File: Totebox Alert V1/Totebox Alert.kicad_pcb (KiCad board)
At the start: 2 copper layers, 180 x 100 mm, 48 parts, among them J1 Conn_01x06, J10 Conn_01x02, J12 Conn_01x02, J3 Conn_01x06, J7 Conn_01x02, J8 Conn_01x02, J9 Conn_01x02, SW1 SW_SPST, U3 ESP32-DEVKITC-32UE

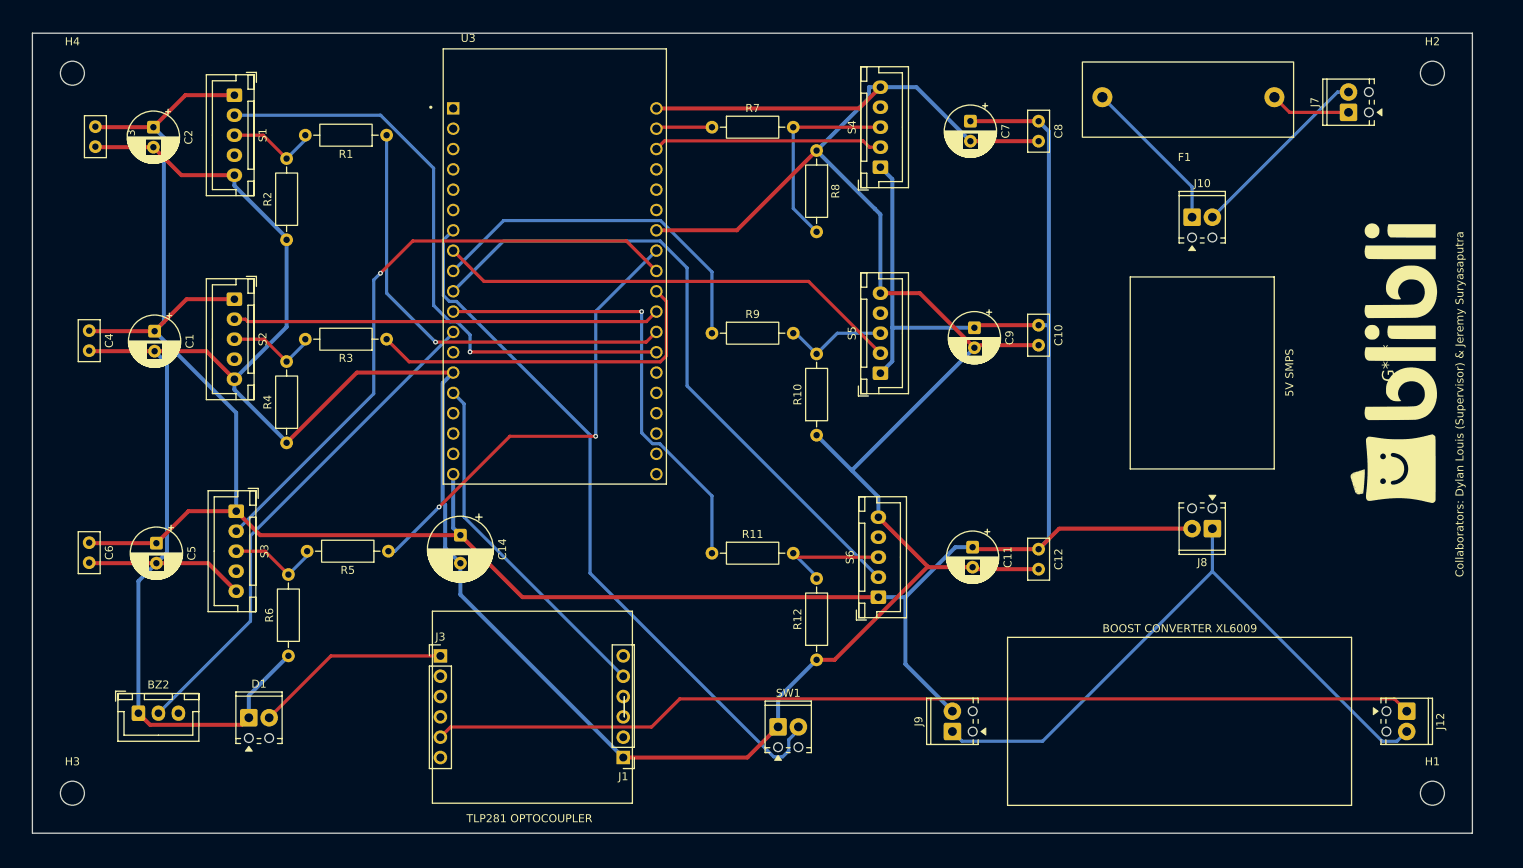
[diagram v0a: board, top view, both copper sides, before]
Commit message: move variables and constants to config.h files for easier configuration and maintenance add new alert tones for multitier floor units categorize mqtt topics to different floor and area units
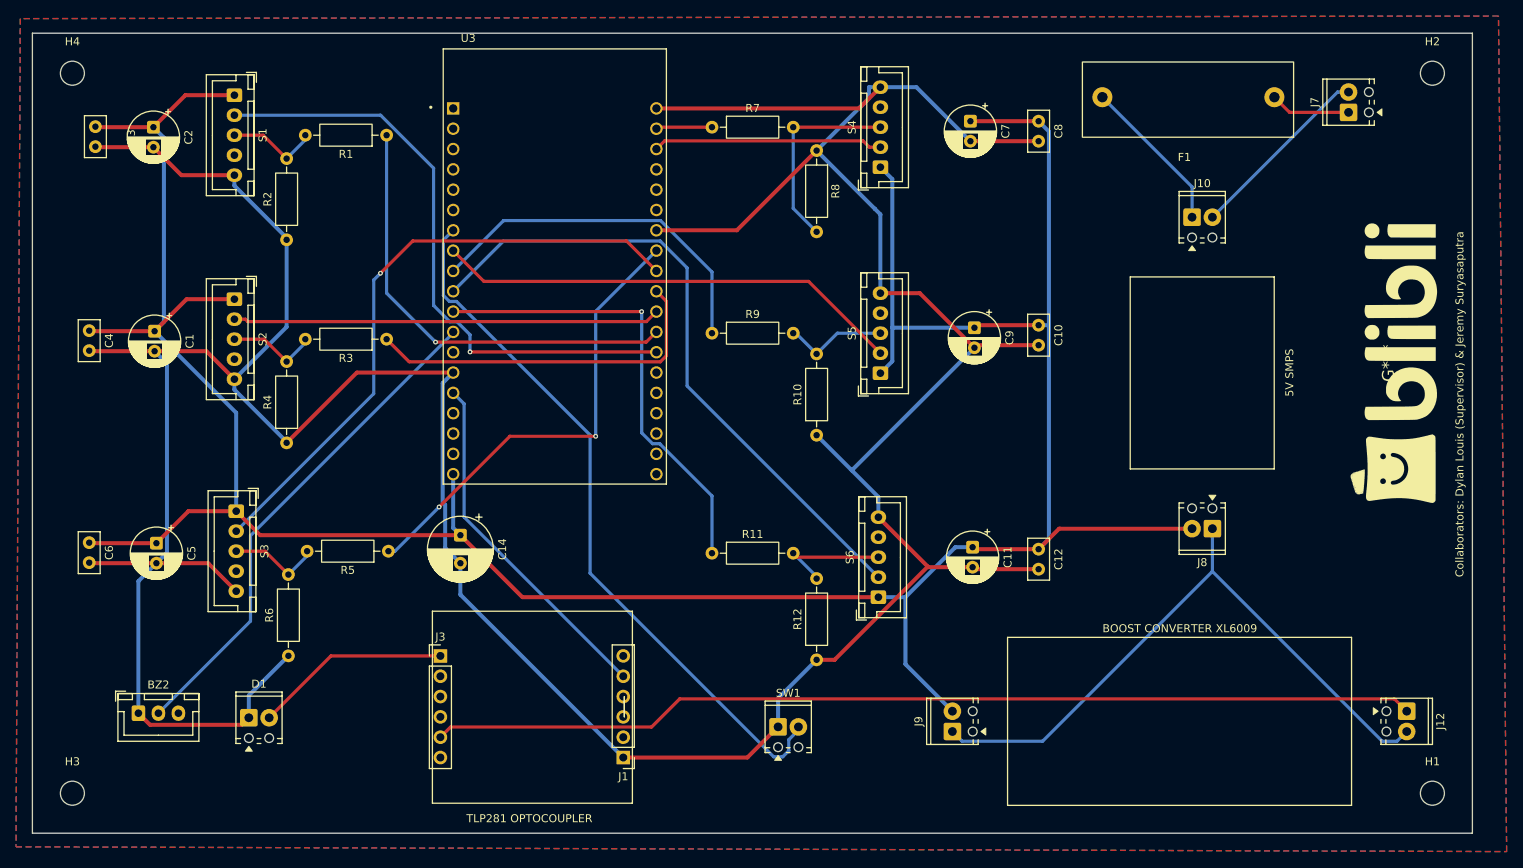
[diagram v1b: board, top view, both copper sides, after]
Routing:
- added copper zone on B.Cu, net (none)
- added copper zone on F.Cu, net (none)
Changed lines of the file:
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@@
+	)
+	(gr_rect
+		(start 86.5 98.5)
+		(end 111.5 122.5)
+		(stroke
+			(width 0.1)
+			(type default)
+		)
+		(fill no)
+		(layer "F.SilkS")
+	)
+	(gr_rect
+		(start 110.491667 109.18)
+		(end 110.491667 111.7)
+		(stroke
+			(width 0.1)
+			(type default)
+		)
+		(fill no)
+		(layer "F.SilkS")
+	)
+	(gr_rect
+		(start 158.395 101.77)
+		(end 201.395 122.77)
+		(stroke
+			(width 0.1)
+			(type default)
+		)
+		(fill no)
+		(layer "F.SilkS")
 	)
 	(gr_rect
@@
 	)
 	(gr_rect
-		(start 110.491667 109.18)
-		(end 110.491667 111.7)
-		(stroke
-			(width 0.1)
-			(type default)
-		)
-		(fill no)
-		(layer "F.SilkS")
-	)
-	(gr_rect
-		(start 158.395 101.77)
-		(end 201.395 122.77)
-		(stroke
-			(width 0.1)
-			(type default)
-		)
-		(fill no)
-		(layer "F.SilkS")
-	)
-	(gr_rect
-		(start 86.5 98.5)
-		(end 111.5 122.5)
-		(stroke
-			(width 0.1)
-			(type default)
-		)
-		(fill no)
-		(layer "F.SilkS")
-	)
-	(gr_rect
 		(start 36.5 26.25)
 		(end 216.5 126.25)
@@
 		(fill no)
 		(layer "Edge.Cuts")
+	)
+	(gr_text "TLP281 OPTOCOUPLER"
+		(at 90.75 125 0)
+		(layer "F.SilkS")
+		(effects
+			(font
+				(size 1 1)
+				(thickness 0.1)
+			)
+			(justify left bottom)
+		)
 	)
 	(gr_text "BOOST CONVERTER XL6009"
@@
 		)
 	)
-	(gr_text "TLP281 OPTOCOUPLER"
-		(at 90.75 125 0)
+	(gr_text "5V SMPS"
+		(at 194.23 71.6825 90)
 		(layer "F.SilkS")
 		(effects
@@
 		)
 	)
-	(gr_text "5V SMPS"
-		(at 194.23 71.6825 90)
-		(layer "F.SilkS")
-		(effects
-			(font
-				(size 1 1)
-				(thickness 0.1)
-			)
-			(justify left bottom)
-		)
-	)
 	(segment
 		(start 142.25 96.75)
@@
 		(net 56)
 	)
+	(zone
+		(net 0)
+		(net_name "")
+		(layers "F.Cu" "B.Cu")
+		(hatch edge 0.5)
+		(connect_pads
+			(clearance 0.5)
+		)
+		(min_thickness 0.25)
+		(filled_areas_thickness no)
+		(fill yes
+			(thermal_gap 0.5)
+			(thermal_bridge_width 0.5)
+			(island_removal_mode 1)
+			(island_area_min 10)
+		)
+		(polygon
+			(pts
+				(xy 34.99 24.43) (xy 34.45 127.95) (xy 220.78 128.55) (xy 219.76 24.1)
+			)
+		)
+	)
 	(embedded_fonts no)
